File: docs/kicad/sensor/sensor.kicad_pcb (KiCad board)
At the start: 2 copper layers, 29.2 x 21.6 mm, 12 parts, among them J1 Conn_01x03, U1 LM393

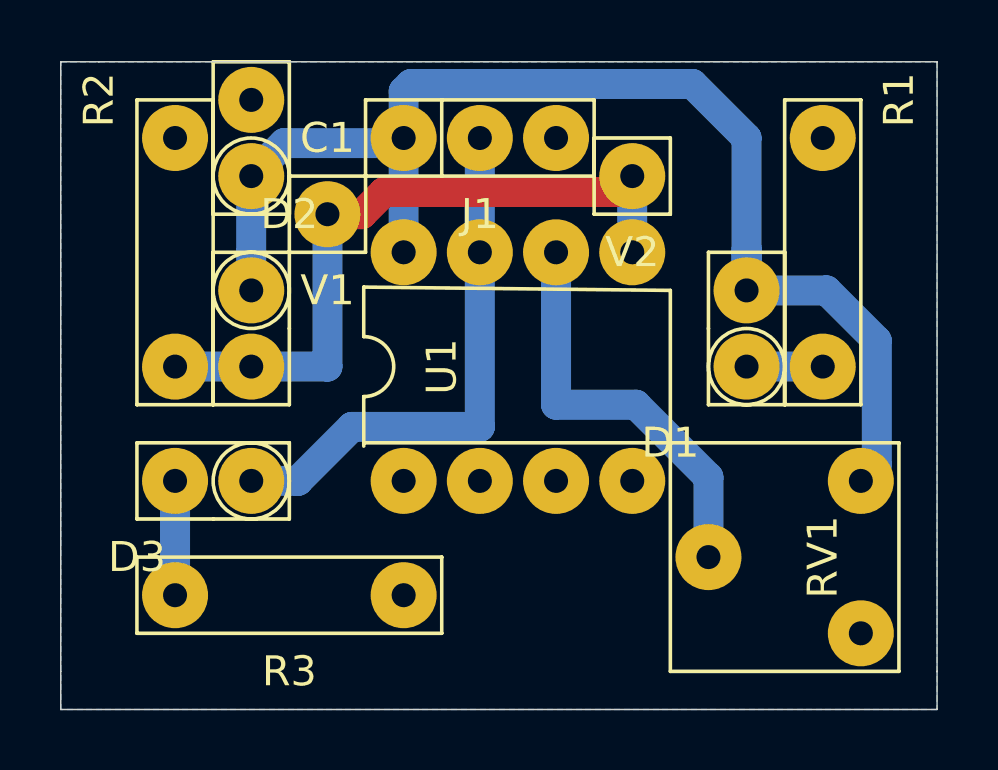
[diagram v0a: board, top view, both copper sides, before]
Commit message: update CNC3018_ESP and other denormalized kiCad stuff*
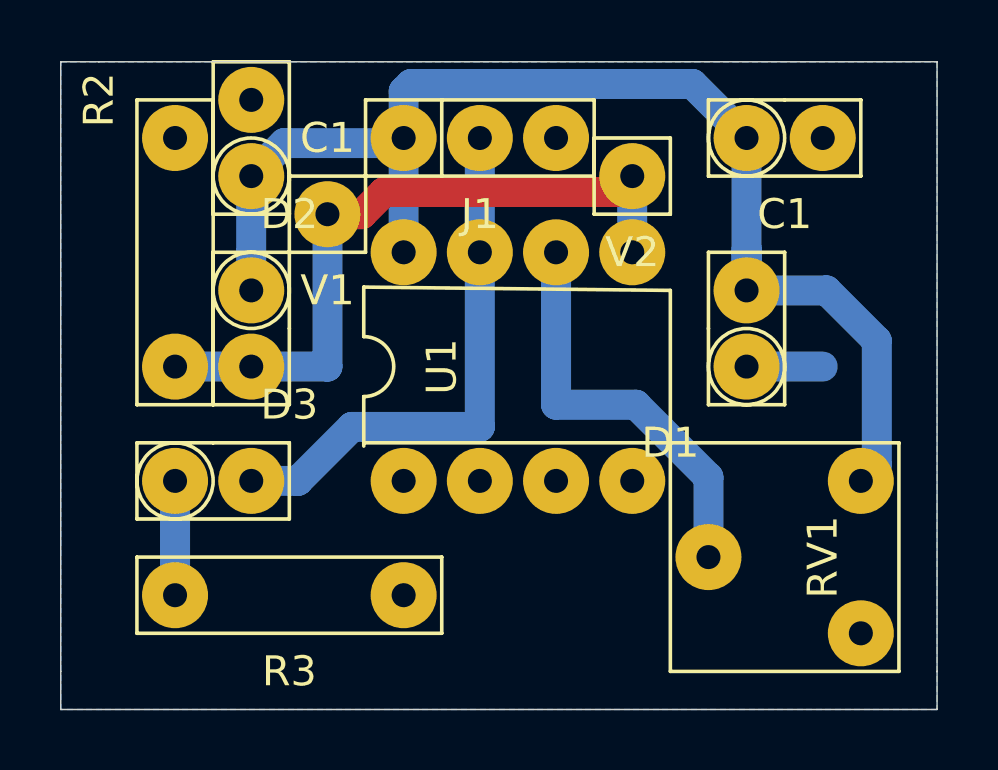
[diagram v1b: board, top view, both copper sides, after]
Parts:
- removed R1: 100, cnc3018-PCB:myResistor
- added C1: 100nf, cnc3018-PCB:my2pin, F.Cu at (22.9, -19.1)
- D1: value IR_Emit -> IR Emit
- moved D3 2.54 mm to (3.81, -7.62), turned to 0 degrees
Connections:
- J1 pad 2: Net-(D3-Pad1) -> Net-(D3-Pad2)
- R3 pad 2: Net-(D3-Pad2) -> Net-(D3-Pad1)
- U1 pad 7: Net-(D3-Pad1) -> Net-(D3-Pad2)
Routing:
- net Net-(D3-Pad2): track 3.81 -> 18.1 mm
- net Net-(D3-Pad1): track 18.1 -> 3.81 mm
